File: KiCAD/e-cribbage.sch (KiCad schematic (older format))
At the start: 569 parts, among them J1 Conn_01x04_Female, U1 74HC595D_118, U10 74HC595D_118, U11 74HC595D_118, U12 74HC595D_118, U13 74HC595D_118, U14 74HC595D_118, U15 74HC595D_118, U16 74HC595D_118, U17 74HC595D_118, U18 74HC595D_118, U19 74HC595D_118, U2 MSP430F2012IPW, U20 74HC595D_118, U21 74HC595D_118, U22 74HC595D_118, U23 74HC595D_118, U24 74HC595D_118, U25 74HC595D_118, U26 74HC595D_118, U27 74HC595D_118, U28 74HC595D_118, U29 74HC595D_118, U3 74HC595D_118, U30 74HC595D_118, U31 74HC595D_118, U32 SN74LVC1G08DBVR, U34 SN74LVC1G08DBVR, U35 SN74LVC1G08DBVR, U36 SN74LVC1G08DBVR, U37 SN74LVC1G08DBVR, U38 SN74LVC1G08DBVR, U39 SN74LVC1G08DBVR, U4 74HC595D_118, U40 SN74LVC1G08DBVR, U5 74HC595D_118, U6 74HC595D_118, U7 74HC595D_118, U8 74HC595D_118, U9 74HC595D_118

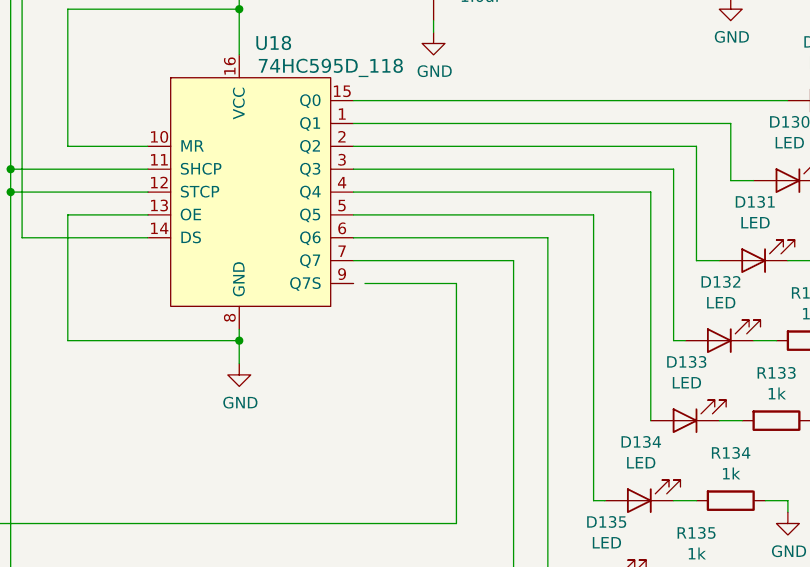
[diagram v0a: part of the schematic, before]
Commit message: schematic fix + more clock routes
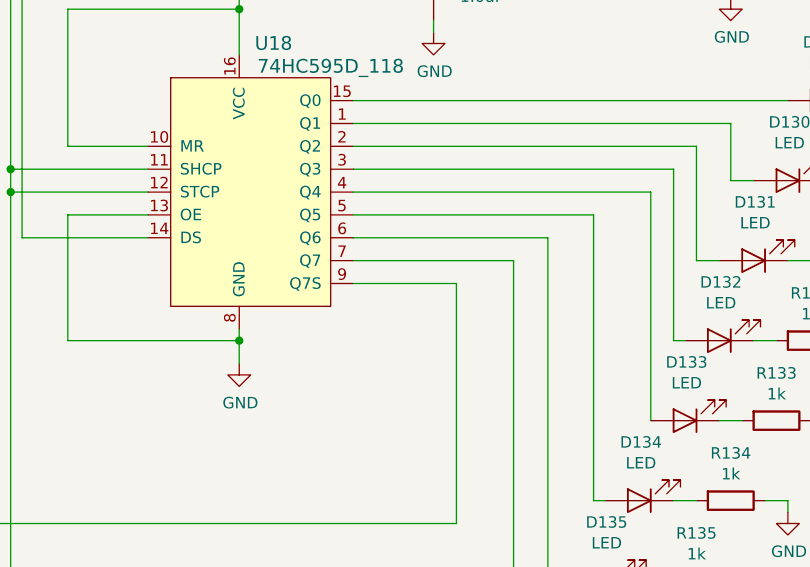
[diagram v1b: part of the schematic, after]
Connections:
- net at U18.9 (Q7S): now also U19.14 (DS)
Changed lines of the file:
@@
 	19950 5500 20500 5500
-Wire Wire Line
-	21450 5700 21850 5700
 Wire Wire Line
 	21850 5700 21850 6750
@@
 Wire Wire Line
 	25400 5950 25400 6050
+Wire Wire Line
+	21400 5700 21850 5700
 $EndSCHEMATC

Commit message: Schematic Update: USB Connector, Power Switch, Load Switch
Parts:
- added C40, C41: 1.0uF, Capacitors_SMD:C_0603_HandSoldering, symbol Device:C
- added J2: USB_B_Micro, Connector_USB:USB_Micro-B_Molex_47346-0001, symbol Connector:USB_B_Micro
- added S5: EG1218, digikey-footprints:Switch_Slide_11.6x4mm_EG1218, symbol dk_Slide-Switches:EG1218
- added U33: TPS22929D, Package_TO_SOT_SMD:SOT-23-6, symbol Power_Management:TPS22929D
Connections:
- net +3V3: now also C41.1, U33.1 (VOUT); no longer BAT1.1, C2.1, J1.1 (Pin_1), R243.2, R244.2, R246.2, R247.2, R251.2, U2.1 (VCC)
- net GND: now also C40.2, C41.2, J2.5 (GND), J2.6 (Shield), U33.2 (GND), U33.5 (GND)
- net at U2.9 (A7/SDI/SDA/TDO/TDI/P1.7): now also U33.3 (ON)
- new net: J2.1 (VBUS), S5.3
- new net +BATT: BAT1.1, S5.1
- new net VS: C2.1, C40.1, J1.1 (Pin_1), R243.2, R244.2, R246.2, R247.2, R251.2, S5.2, U2.1 (VCC), U33.4 (VIN), U33.6 (VIN)
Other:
- moved on the sheet: BAT1, C2, C32, C33, C34, C35, C36, C37, C38, C39, J1, R243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

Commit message: schematic updates - added 3.3V Linear Regulator
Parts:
- added U41: LM317T, digikey-footprints:TO-220-3, symbol dk_PMIC-Voltage-Regulators-Linear:LM317T
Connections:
- wire segments 2206 -> 2207
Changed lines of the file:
@@
 	1800 2450 1800 2500
-Wire Wire Line
-	2200 1800 2850 1800
-Wire Wire Line
-	2850 1800 2850 2900
-Wire Wire Line
-	2850 2900 3900 2900
 Wire Wire Line
 	1800 3100 3900 3100
@@
 	4600 8900 4600 9000
 Connection ~ 4600 8900
+$Comp
+L dk_PMIC-Voltage-Regulators-Linear:LM317T U41
+U 1 1 5F6E0963
+P 3250 1800
+F 0 "U41" H 3250 2087 60  0000 C CNN
+F 1 "LM317T" H 3250 1981 60  0000 C CNN
+F 2 "digikey-footprints:TO-220-3" H 3450 2000 60  0001 L CNN
+F 3 "http://www.st.com/content/ccc/resource/technical/document/datasheet/group1/a0/db/e6/9b/6f/9c/45/7b/CD00000455/files/CD00000455.pdf/jcr:content/translations/en.CD00000455.pdf" H 3450 2100 60  0001 L CNN
+F 4 "497-1575-5-ND" H 3450 2200 60  0001 L CNN "Digi-Key_PN"
+F 5 "LM317T" H 3450 2300 60  0001 L CNN "MPN"
+F 6 "Integrated Circuits (ICs)" H 3450 2400 60  0001 L CNN "Category"
+F 7 "PMIC - Voltage Regulators - Linear" H 3450 2500 60  0001 L CNN "Family"
+F 8 "http://www.st.com/content/ccc/resource/technical/document/datasheet/group1/a0/db/e6/9b/6f/9c/45/7b/CD00000455/files/CD00000455.pdf/jcr:content/translations/en.CD00000455.pdf" H 3450 2600 60  0001 L CNN "DK_Datasheet_Link"
+F 9 "/product-detail/en/stmicroelectronics/LM317T/497-1575-5-ND/591677" H 3450 2700 60  0001 L CNN "DK_Detail_Page"
+F 10 "IC REG LIN POS ADJ 1.5A TO220AB" H 3450 2800 60  0001 L CNN "Description"
+F 11 "STMicroelectronics" H 3450 2900 60  0001 L CNN "Manufacturer"
+F 12 "Active" H 3450 3000 60  0001 L CNN "Status"
+	1    3250 1800
+	1    0    0    -1
+$EndComp
+$Comp
+L power:GND #PWR0371
+U 1 1 5F6E21CF
+P 3250 2100
+F 0 "#PWR0371" H 3250 1850 50  0001 C CNN
+F 1 "GND" H 3255 1927 50  0000 C CNN
+F 2 "" H 3250 2100 50  0001 C CNN
+F 3 "" H 3250 2100 50  0001 C CNN
+	1    3250 2100
+	1    0    0    -1
+$EndComp
+Wire Wire Line
+	2200 1800 2950 1800
+Wire Wire Line
+	3550 1800 3650 1800
+Wire Wire Line
+	3650 1800 3650 2900
+Wire Wire Line
+	3650 2900 3900 2900
 $EndSCHEMATC

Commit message: Schematic Updates - SMT Batt/USB switch, 3.3V LDO, RCLCK connections to shift regs Library Updates - added 3D models for switches and battery
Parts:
- removed U41: LM317T, digikey-footprints:TO-220-3, symbol dk_PMIC-Voltage-Regulators-Linear:LM317T
- added C42, C43: 1.0uF, Capacitor_SMD:C_0603_1608Metric_Pad1.05x0.95mm_HandSolder, symbol Device:C
- added U41: TLV71333PDBV, Package_TO_SOT_SMD:SOT-23-5, symbol Regulator_Linear:TLV71333PDBV
- C1, C10, C11, C12, C13, C14, C15, C16, C17, C18, C19, C2, C20, C21, C22, C23, C24, C25, C26, C27, C28, C29, C3, C30, C31, C32, C33, C34, C35, C36, C37, C38, C39, C4, C40, C41, C5, C6, C7, C8, C9: footprint Capacitors_SMD:C_0603_HandSoldering -> Capacitor_SMD:C_0603_1608Metric_Pad1.05x0.95mm_HandSolder
- S5: footprint digikey-footprints:Switch_Slide_11.6x4mm_EG1218 -> Button_Switch_SMD:SW_SPDT_CK-JS102011SAQN
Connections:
- net labels added: RCLK
- wire segments 2207 -> 2219

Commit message: fixed broken connection on U24-14
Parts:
- S5: symbol dk_Slide-Switches:EG1218 -> e-cribbage-rescue:EG1218-dk_Slide-Switches
- U41: symbol Regulator_Linear:TLV71333PDBV -> e-cribbage-rescue:TLV71333PDBV-Regulator_Linear
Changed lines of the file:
@@
 EESchema Schematic File Version 4
+LIBS:e-cribbage-cache
 EELAYER 30 0
 EELAYER END
@@
 	24300 20000 24300 2550
 Wire Wire Line
-	26000 2750 26450 2750
-Wire Wire Line
 	26450 2750 26450 3900
 Wire Wire Line
 	26450 3900 24650 3900
 Wire Wire Line
-	24650 5500 25000 5500
-Wire Wire Line
 	25900 5700 26350 5700
 Wire Wire Line
@@
 $EndComp
 $Comp
-L dk_Slide-Switches:EG1218 S5
+L e-cribbage-rescue:EG1218-dk_Slide-Switches S5
 U 1 1 5F54CAD8
 P 4100 3000
@@
 	19900 5200 19900 8250
 $Comp
-L Regulator_Linear:TLV71333PDBV U41
+L e-cribbage-rescue:TLV71333PDBV-Regulator_Linear U41
 U 1 1 6DF80E45
 P 3250 1900
@@
 Wire Wire Line
 	5050 6800 3950 6800
+Wire Wire Line
+	25000 5500 24650 5500
+Wire Wire Line
+	25950 2750 26450 2750
 $EndSCHEMATC

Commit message: schematic and parts cleanup
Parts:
- C1, C10, C11, C12, C13, C14, C15, C16, C17, C18, C19, C2, C20, C21, C22, C23, C24, C25, C26, C27, C28, C29, C3, C30, C31, C32, C33, C34, C35, C36, C37, C38, C39, C4, C5, C6, C7, C8, C9: value 1.0uF -> 0.1uF
- D1, D10, D100, D101, D102, D103, D104, D105, D106, D107, D108, D109, D11, D110, D111, D112, D113, D114, D115, D116, D117, D118, D119, D12, D120, D13, D14, D15, D16, D17, D18, D19, D2, D20, D21, D22, D23, D24, D25, D26, D27, D28, D29, D3, D30, D31, D32, D33, D34, D35, D36, D37, D38, D39, D4, D40, D41, D42, D43, D44, D45, D46, D47, D48, D49, D5, D50, D51, D52, D53, D54, D55, D56, D57, D58, D59, D6, D60, D61, D62, D63, D64, D65, D66, D67, D68, D69, D7, D70, D71, D72, D73, D74, D75, D76, D77, D78, D79, D8, D80, D81, D82, D83, D84, D85, D86, D87, D88, D89, D9, D90, D91, D92, D93, D94, D95, D96, D97, D98, D99: value LED -> LED1
- D121, D122, D123, D124, D125, D126, D127, D128, D129, D130, D131, D132, D133, D134, D135, D136, D137, D138, D139, D140, D141, D142, D143, D144, D145, D146, D147, D148, D149, D150, D151, D152, D153, D154, D155, D156, D157, D158, D159, D160, D161, D162, D163, D164, D165, D166, D167, D168, D169, D170, D171, D172, D173, D174, D175, D176, D177, D178, D179, D180, D181, D182, D183, D184, D185, D186, D187, D188, D189, D190, D191, D192, D193, D194, D195, D196, D197, D198, D199, D200, D201, D202, D203, D204, D205, D206, D207, D208, D209, D210, D211, D212, D213, D214, D215, D216, D217, D218, D219, D220, D221, D222, D223, D224, D225, D226, D227, D228, D229, D230, D231, D232, D233, D234, D235, D236, D237, D238, D239, D240: value LED -> LED2

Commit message: library and layout cleanup
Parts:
- C1, C10, C11, C12, C13, C14, C15, C16, C17, C18, C19, C2, C20, C21, C22, C23, C24, C25, C26, C27, C28, C29, C3, C30, C31, C32, C33, C34, C35, C36, C37, C38, C39, C4, C40, C41, C42, C43, C5, C6, C7, C8, C9: footprint Capacitor_SMD:C_0603_1608Metric_Pad1.05x0.95mm_HandSolder -> e-cribbage:C_0603_1608Metric_Pad1.05x0.95mm_HandSolder
- S1, S2, S3, S4: footprint Buttons_Switches_SMD:SW_SPST_B3SL-1002P -> w_switch:KS12R22
- U1, U10, U11, U12, U13, U14, U15, U16, U17, U18, U19, U20, U21, U22, U23, U24, U25, U26, U27, U28, U29, U3, U30, U31, U4, U5, U6, U7, U8, U9: footprint digikey-footprints:TSSOP-16_W4.40mm -> e-cribbage:TSSOP-16_W4.40mm
